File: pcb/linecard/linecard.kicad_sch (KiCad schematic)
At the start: 0 parts

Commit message: Hopefully finished first PHY
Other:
- added sheet PHY 0 Backend (phy0.kicad_sch)
- added sheet PHY 0 MDI (phy0_mdi.kicad_sch)
- added sheet PHY 0 Power (phy0_pwr.kicad_sch)
- sheet Power Supply ports: added 3V3, PHY0_PWRDN, PHY0_RST, PHY1_PWRDN, PHY1_RST; removed none
- note removed: "JTAG is 3.3V tolerant, but runs at 2.5V levels"

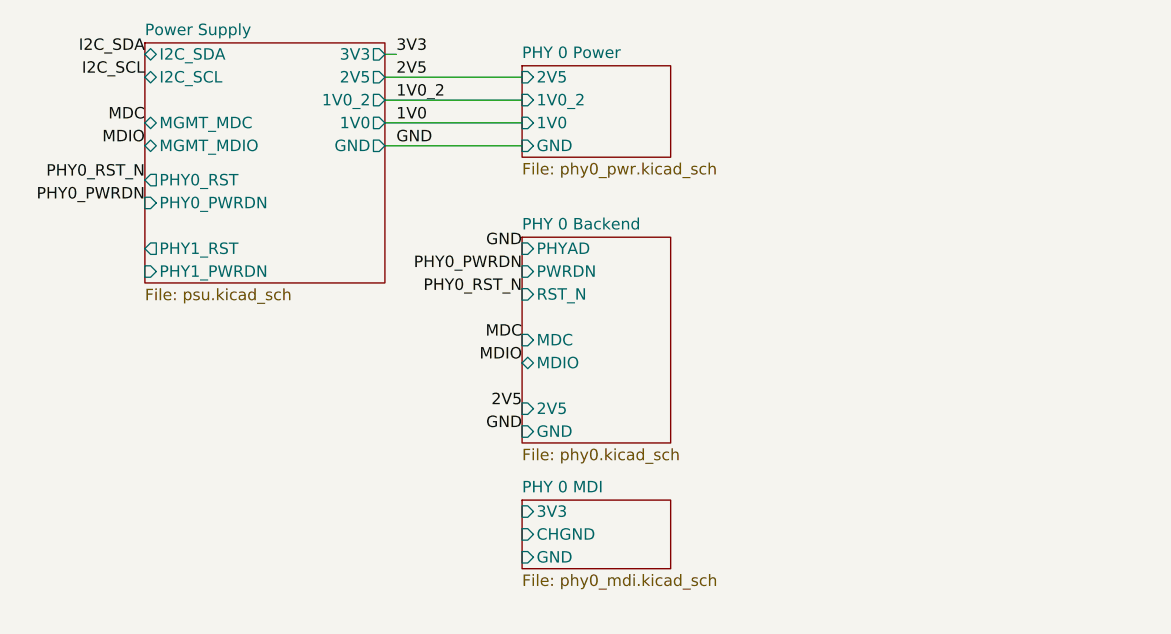
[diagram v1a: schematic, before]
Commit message: Finished initial schematic of line card
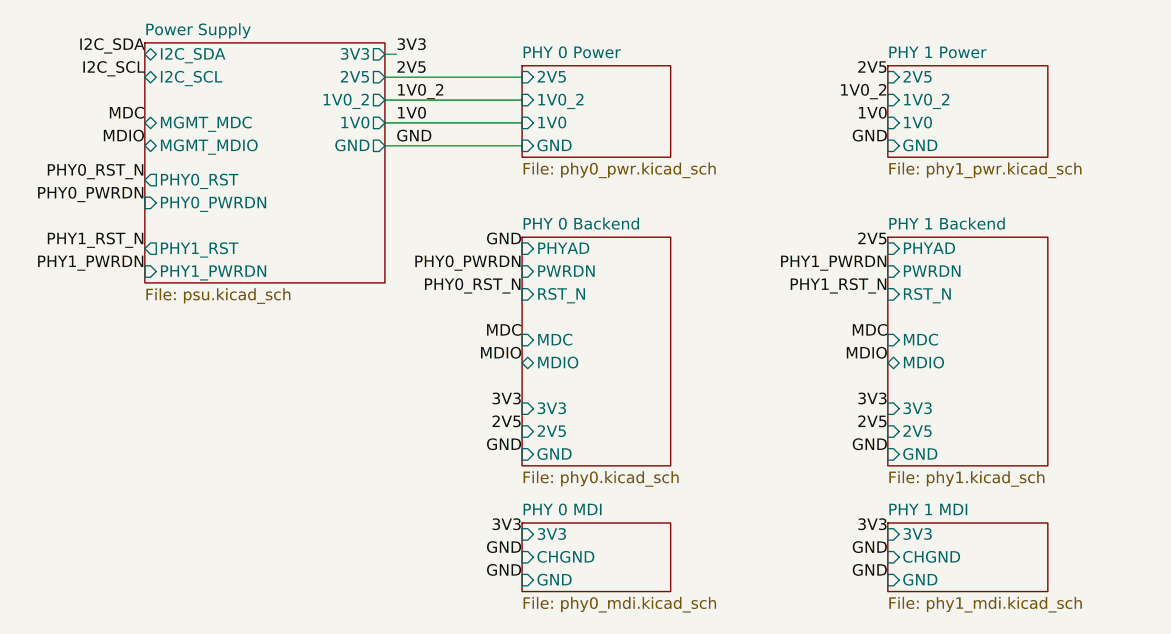
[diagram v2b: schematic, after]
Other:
- added sheet PHY 1 Backend (phy1.kicad_sch)
- added sheet PHY 1 MDI (phy1_mdi.kicad_sch)
- added sheet PHY 1 Power (phy1_pwr.kicad_sch)
- sheet PHY 0 Backend ports: added 3V3; removed none

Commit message: Added heatsink, some silkscreen logos, mounting holes, and ground clips
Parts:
- added M1: LONGTHING, azonenberg_pcb:LONGTHING-1200DPI, symbol special-azonenberg:MECHANICAL
- added M10, M11, M4, M5, M6, M7, M8, M9: SCREWHOLE, azonenberg_pcb:MECHANICAL_CLEARANCEHOLE_4_40, symbol conn:CONN_01X01
- added M2: OSHW, w_logo:Logo_silk_OSHW_6x6mm, symbol special-azonenberg:MECHANICAL
- added M3: WEEE, w_logo:Logo_silk_WEEE_3.4x5mm, symbol special-azonenberg:MECHANICAL
- added TP1, TP2, TP21, TP4: GROUNDCLIP, azonenberg_pcb:TESTPOINT_SMT_KEYSTONE_5016, symbol conn:CONN_01X01
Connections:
- net GND: now also M10.1 (P1), M11.1 (P1), M4.1 (P1), M5.1 (P1), M6.1 (P1), M7.1 (P1), M8.1 (P1), M9.1 (P1), TP1.1 (P1), TP2.1 (P1), TP21.1 (P1), TP4.1 (P1)
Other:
- sheet Power Supply ports: added none; removed I2C_SCL, I2C_SDA
- note added: "Debug ground points (may add more at layout time)"
- note added: "MDIO addr: 0-11"
- note added: "MDIO addr: 12-23"
- note added: "Mounting holes"
- note added: "Silkscreen logos"

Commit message: Finished initial schematic review
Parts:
- added R100: 1K, symbol device:R
- added R101: 10K, symbol device:R
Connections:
- net 2V5: now also R100.2, R101.2
- net MDC: now also R101.1
- net MDIO: now also R100.1
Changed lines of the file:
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@@
 	(title_block
 		(title "LATENTRED Line Card")
-		(date "2024-12-10")
+		(date "2024-12-11")
 		(rev "0.1")
 		(company "Antikernel Labs")
@@
 		)
 	)
+	(label "2V5"
+		(at 90.17 100.33 0)
+		(fields_autoplaced yes)
+		(effects
+			(font
+				(size 1.27 1.27)
+			)
+			(justify left bottom)
+		)
+	)
 	(label "3V3"
 		(at 123.19 57.15 180)
@@
 	)
 	(label "MDC"
+		(at 82.55 100.33 180)
+		(fields_autoplaced yes)
+		(effects
+			(font
+				(size 1.27 1.27)
+			)
+			(justify right bottom)
+		)
+	)
+	(label "MDC"
 		(at 123.19 49.53 180)
 		(fields_autoplaced yes)
@@
 		)
 	)
+	(label "MDIO"
+		(at 82.55 95.25 180)
+		(fields_autoplaced yes)
+		(effects
+			(font
+				(size 1.27 1.27)
+			)
+			(justify right bottom)
+		)
+	)
 	(label "PHY1_PWRDN"
 		(at 123.19 41.91 180)
@@
 			)
 			(justify right bottom)
+		)
+	)
+	(label "2V5"
+		(at 90.17 95.25 0)
+		(fields_autoplaced yes)
+		(effects
+			(font
+				(size 1.27 1.27)
+			)
+			(justify left bottom)
 		)
 	)
@@
 	)
 	(symbol
+		(lib_id "device:R")
+		(at 86.36 95.25 90)
+		(unit 1)
+		(exclude_from_sim no)
+		(in_bom yes)
+		(on_board yes)
+		(dnp no)
+		(property "Reference" "R100"
+			(at 86.36 92.71 90)
+			(effects
+				(font
+					(size 1.27 1.27)
+				)
+			)
+		)
+		(property "Value" "1K"
+			(at 86.36 95.25 90)
+			(effects
+				(font
+					(size 1.27 1.27)
+				)
+			)
+		)
+		(property "Footprint" ""
+			(at 86.36 97.028 90)
+			(effects
+				(font
+					(size 1.27 1.27)
+				)
+				(hide yes)
+			)
+		)
+		(property "Datasheet" ""
+			(at 86.36 95.25 0)
+			(effects
+				(font
+					(size 1.27 1.27)
+				)
+				(hide yes)
+			)
+		)
+		(property "Description" "Resistor"
+			(at 86.36 95.25 0)
+			(effects
+				(font
+					(size 1.27 1.27)
+				)
+				(hide yes)
+			)
+		)
+		(pin "2"
+		)
+		(pin "1"
+		)
+		(instances
+			(project ""
+				(path "/a55ad1ec-4cad-4d06-8b73-31c98dcc1d79"
+					(reference "R100")
+					(unit 1)
+				)
+			)
+		)
+	)
+	(symbol
 		(lib_id "conn:CONN_01X01")
 		(at 25.4 260.35 0)
@@
 					(unit 1)
 				)
+			)
+		)
+	)
+	(symbol
+		(lib_id "device:R")
+		(at 86.36 100.33 90)
+		(unit 1)
+		(exclude_from_sim no)
+		(in_bom yes)
+		(on_board yes)
+		(dnp no)
+		(property "Reference" "R101"
+			(at 86.36 97.79 90)
+			(effects
+				(font
+					(size 1.27 1.27)
+				)
+			)
+		)
+		(property "Value" "10K"
+			(at 86.36 100.33 90)
+			(effects
+				(font
+					(size 1.27 1.27)
+				)
+			)
+		)
+		(property "Footprint" ""
+			(at 86.36 102.108 90)
+			(effects
+				(font
+					(size 1.27 1.27)
+				)
+				(hide yes)
+			)
+		)
+		(property "Datasheet" ""
+			(at 86.36 100.33 0)
+			(effects
+				(font
+					(size 1.27 1.27)
+				)
+				(hide yes)
+			)
+		)
+		(property "Description" "Resistor"
+			(at 86.36 100.33 0)
+			(effects
+				(font
+					(size 1.27 1.27)
+				)
+				(hide yes)
+			)
+		)
+		(pin "2"
+		)
+		(pin "1"
+		)
+		(instances
+			(project "linecard"
+				(path "/a55ad1ec-4cad-4d06-8b73-31c98dcc1d79"
+					(reference "R101")
+					(unit 1)
+				)

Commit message: Began layout of first few ports and left VSC8512
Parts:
- R100, R101: footprint (none) -> azonenberg_pcb:EIA_0402_RES_NOSILK
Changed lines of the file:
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@@
 			)
 		)
-		(property "Footprint" ""
+		(property "Footprint" "azonenberg_pcb:EIA_0402_RES_NOSILK"
 			(at 86.36 97.028 90)
 			(effects
@@
 			)
 		)
-		(property "Footprint" ""
+		(property "Footprint" "azonenberg_pcb:EIA_0402_RES_NOSILK"
 			(at 86.36 102.108 90)
 			(effects

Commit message: Preliminary placement of ESD diodes for right PHY
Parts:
- M1: footprint azonenberg_pcb:LONGTHING-1200DPI -> azonenberg_pcb:LONGTHING-600DPI
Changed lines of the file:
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@@
 			)
 		)
-		(property "Footprint" "azonenberg_pcb:LONGTHING-1200DPI"
+		(property "Footprint" "azonenberg_pcb:LONGTHING-600DPI"
 			(at 15.24 233.68 0)
 			(effects
